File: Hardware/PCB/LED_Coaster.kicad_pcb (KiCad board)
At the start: 2 copper layers, 90 x 90 mm, 88 parts, among them J1 Li-po, J3 USB_C_Receptacle_USB2.0_16P, J4 UART, Q1 AO3401A, SW1 SW_SPDT, U1 ESP32-C3-WROOM-02-H4, U3 MCP73871-2CC, U4 TLV75533PDBVR

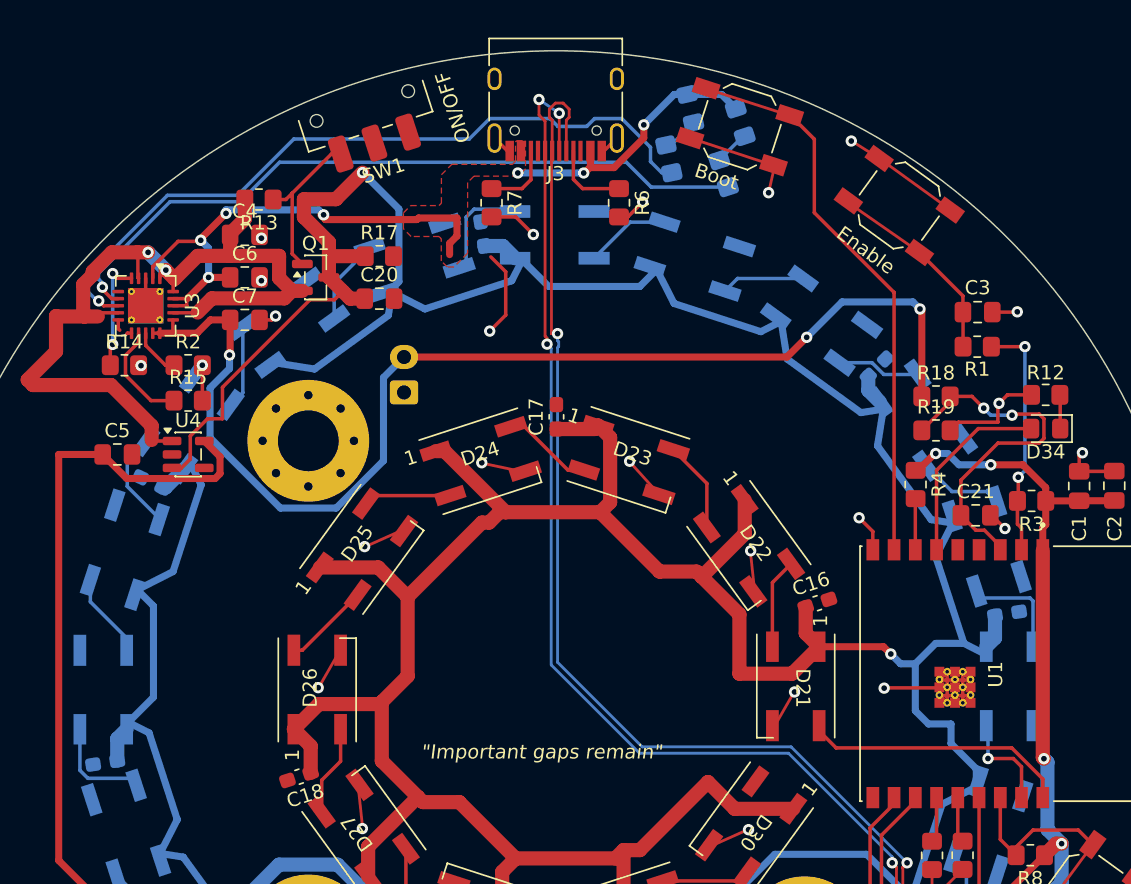
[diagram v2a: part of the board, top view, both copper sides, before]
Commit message: Route charger status to the ESP32 and move the order to Economic
The board reports charge state in firmware now instead of on LEDs. U3's
three open-drain status outputs go to spare ESP32 pins - STAT1/LBO to
IO5, STAT2 to IO6, PG to IO10 - and the status LEDs D33/D35 with their
resistors R5/R16 are deleted.

Deleting them is required, not cosmetic: they pulled STAT1/STAT2 up to
+5V, and the ESP32-C3 is rated 3.6 V max on a pin. PG is what makes the
state decodable at all - per the MCP73871 Table 5-1, charging and low
battery share the same STAT1/STAT2 pair and differ only in PG.

The assembly model changes with it. The order is now Economic, single
sided, front only: 20 BOM lines and 47 placed parts for about $88,
against the $172.46 Standard double-sided quoted. Standard bills the
feeder fee on every line including Basic ones; Economic bills it only on
extended parts. The 28 back-side parts are the outer ring and its
decoupling, hand-soldered in a second stage, leaving J1 as the only part
stage one needs.

D1-D30 move to C55109525 (WS2812B-V7). C2761795 is Standard-only and one
such line forces the whole order off Economic. The V7 keeps the classic
1=VDD 2=DOUT 3=GND 4=DIN pinout so it drops in at 0 degrees; an SK6812
is also Economic-eligible but is 1=GND 2=DIN 3=VDD 4=DOUT, which at 0
degrees reverses the supply and destroys every LED.

C1, C3 and C5 merge onto the 4.7uF line - they were 25 V and 50 V parts
on a 3.3 V rail at twice the price of the 4.7uF already in the BOM.

Routing the three status nets through the B.Cu annulus split the ground
pour; two 1.0 mm bridges reconnect U3's ground island and C7.

Co-Authored-By: Claude Opus 5 <noreply@anthropic.com>
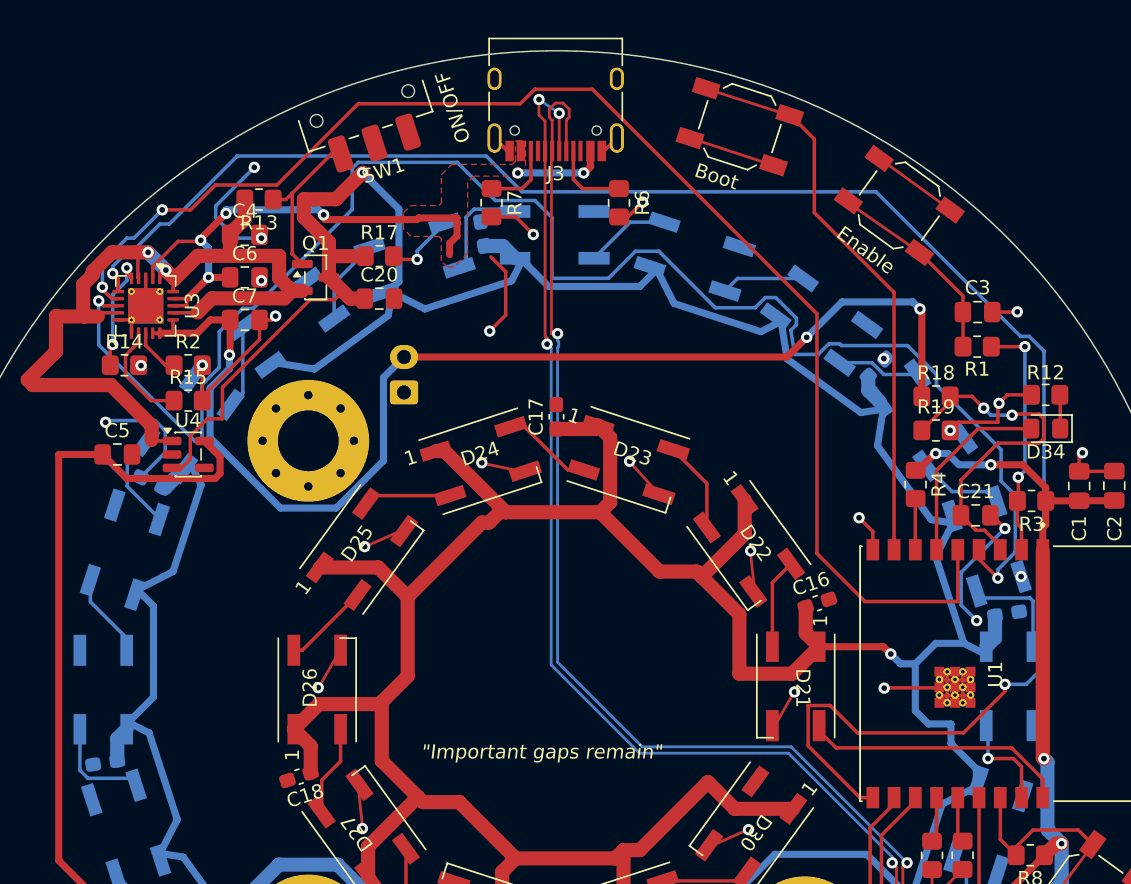
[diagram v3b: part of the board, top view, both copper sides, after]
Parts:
- removed D33, D35: LED, LED_SMD:LED_0805_2012Metric_Pad1.15x1.40mm_HandSolder
- removed R16, R5: 1k, Resistor_SMD:R_0805_2012Metric_Pad1.20x1.40mm_HandSolder
- C1: value 10uF -> 4.7uF
- C3: value 1uF -> 4.7uF
- C5: value 2.2uF -> 4.7uF
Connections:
- U1 pad 10: unconnected-(U1-IO10-Pad10) -> /PG
- U1 pad 4: unconnected-(U1-IO5-Pad4) -> /STAT1
- U1 pad 5: unconnected-(U1-IO6-Pad5) -> /STAT2
- U3 pad 6: unconnected-(U3-~{PG}-Pad6) -> /PG
- U3 pad 7: Net-(U3-STAT2) -> /STAT2
- U3 pad 8: Net-(U3-STAT1/~{LBO}) -> /STAT1
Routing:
- net /PG: track 0.00 -> 127.5 mm, vias 0 -> 2
- net /STAT1: track 0.00 -> 113.6 mm, vias 0 -> 2
- net /STAT2: track 0.00 -> 97.5 mm, vias 0 -> 2
- net Net-(U3-STAT1/~{LBO}): track 52.3 -> 0.00 mm, vias 1 -> 0
- net Net-(U3-STAT2): track 51.1 -> 0.00 mm, vias 1 -> 0
- net GND: track 86.4 -> 126.2 mm, vias 30 -> 35
- net +5V: track 56.4 -> 43.1 mm, vias 7 -> 6
- net Net-(D33-K): track 2.60 -> 0.00 mm
- net Net-(D35-K): track 2.50 -> 0.00 mm

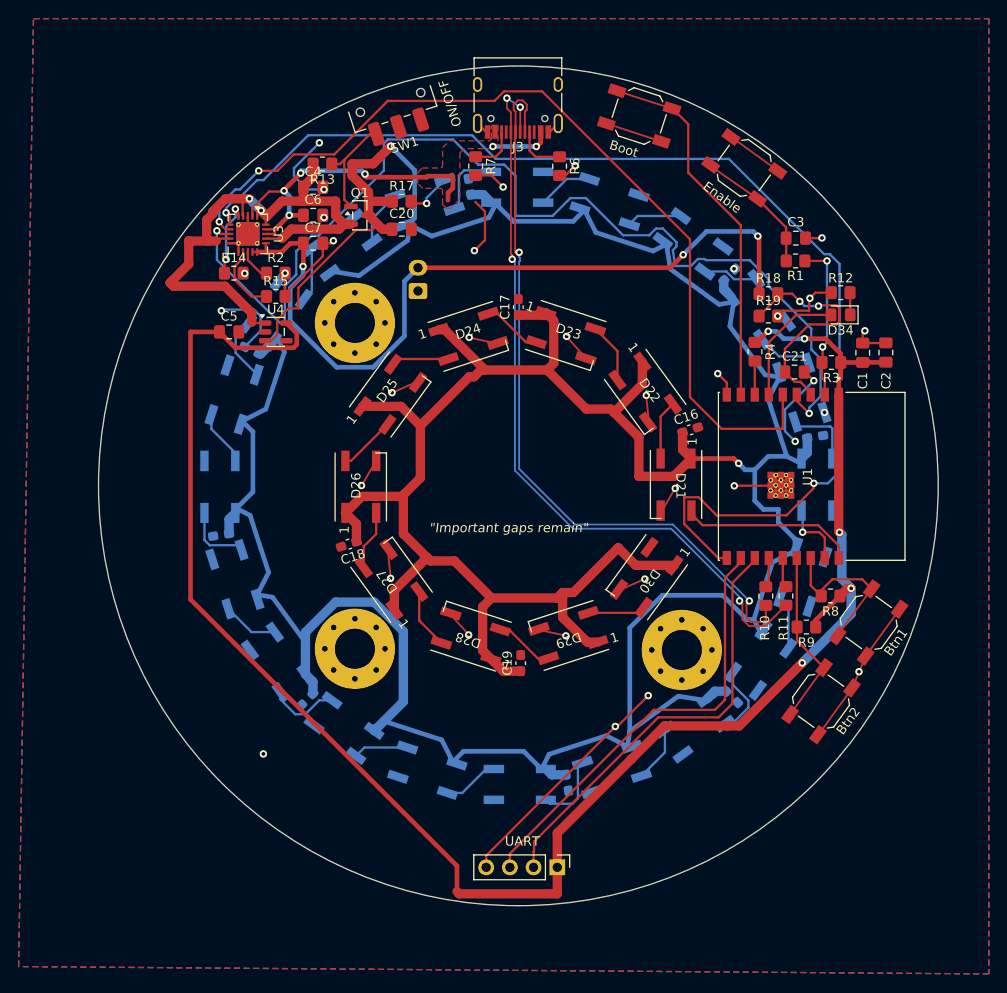
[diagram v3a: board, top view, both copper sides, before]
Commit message: Switch the LEDs to C26167850 and give the back-side parts thermal relief
Every WS2812B is MSL 5a and rated 240 C peak reflow. Economic PCBA runs a
255 C profile and does not bake, so JLCPCB rejects them at cart time no
matter what the part page's PCBA Type field claims - that field is
catalogue metadata, not what the ordering system enforces. C55109525,
C5380881 and both house-brand parts all advertise "Economic and Standard"
and all fail. Only the cart is authoritative.

TUOZHAN TZ-5050S2RGB-5V-I4-H1 clears it: MSL 3, 250 C peak, qualified at
260 C x 10 s twice with 0/22 failures. Verified accepted as Economic.

It is a better part here besides. Classic 1=VDD 2=DOU 3=GND 4=DIN pinout
so it drops in at 0 degrees; 80 us reset instead of 280, which retires the
delay(1) contingency the V7 would have needed; GRB order and bit timing
that FastLED's WS2812 driver already sits inside, so no firmware change at
all. 12 mA/channel against ~18-20 takes full white from ~1.8 A to ~1.08 A,
which largely retires the MCP73871 1 A system-load concern, and it is
brighter on green and blue despite the lower current.

D1-D20 and C8-C15 now carry zone_connect 1. The GND pour is solid, and the
datasheet allows an iron at 315 C for under 3 seconds once only - those
fight each other on a pad tied straight into a plane. Thermal relief on
just the hand-soldered back-side parts leaves the machine-assembled front
reflowing as before and keeps U3's exposed pad solid, as it needs to be.

Ordered: 20 lines, 47 parts, 7 extended. $83.36 PCBA plus $2.00 for the
boards against the $172.46 the first Standard double-sided quote came to.

Co-Authored-By: Claude Opus 5 <noreply@anthropic.com>
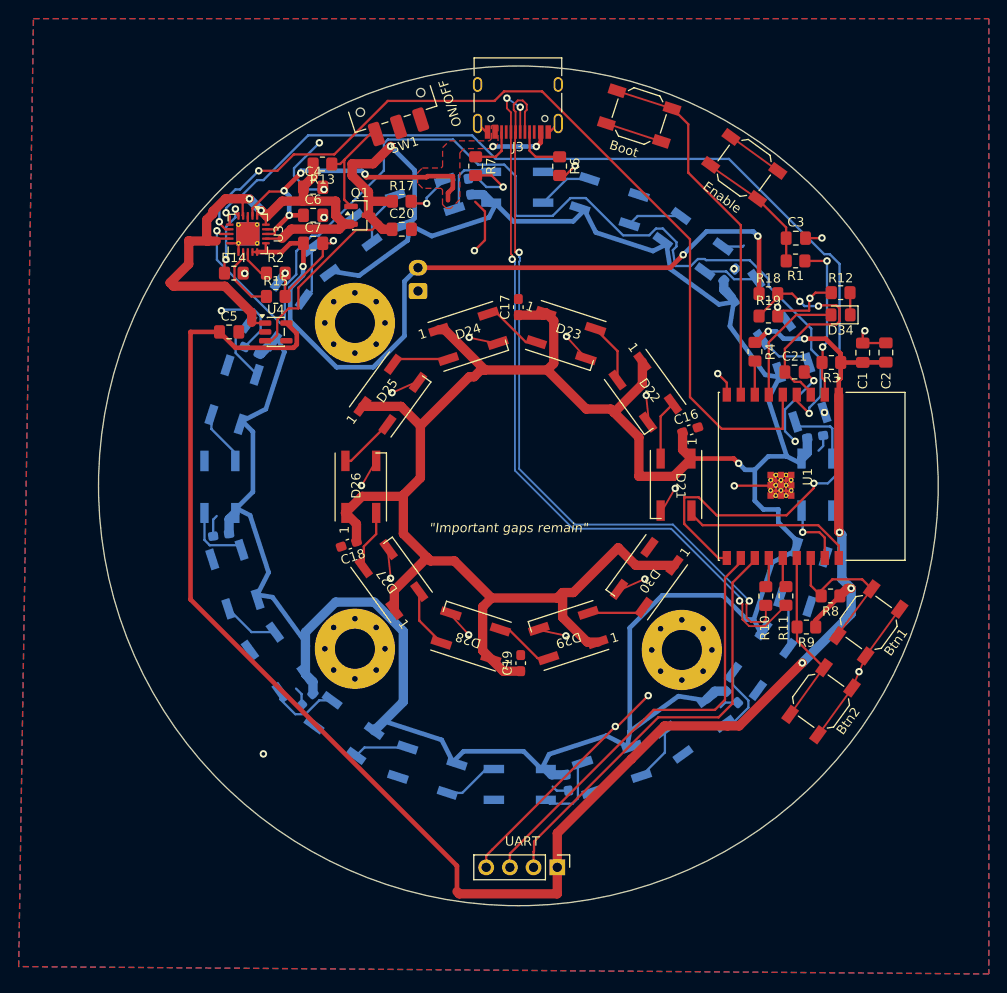
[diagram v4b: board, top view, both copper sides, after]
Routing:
- net GND: track 126.2 -> 143.9 mm
